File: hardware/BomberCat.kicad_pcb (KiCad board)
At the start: 2 copper layers, 0 parts

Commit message: add footprint memory and fix path footprints
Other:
- net class Default removed
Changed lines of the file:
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@@
-(kicad_pcb (version 20171130) (host pcbnew "(5.1.9-0-10_14)")
+(kicad_pcb (version 20211014) (generator pcbnew)
   (general
     (thickness 1.6)
-    (drawings 0)
-    (tracks 0)
-    (zones 0)
-    (modules 0)
-    (nets 1)
   )
-  (page A4)
+  (paper "A4")
   (layers
-    (0 Top signal)
-    (31 Bottom signal)
-    (32 B.Adhes user)
-    (33 F.Adhes user)
-    (34 B.Paste user)
-    (35 F.Paste user)
-    (36 B.SilkS user)
-    (37 F.SilkS user)
-    (38 B.Mask user)
-    (39 F.Mask user)
-    (40 Dwgs.User user)
-    (41 Cmts.User user)
-    (42 Eco1.User user)
-    (43 Eco2.User user)
-    (44 Edge.Cuts user)
-    (45 Margin user)
-    (46 B.CrtYd user)
-    (47 F.CrtYd user)
-    (48 B.Fab user)
-    (49 F.Fab user)
+    (0 "F.Cu" signal "Top")
+    (31 "B.Cu" signal "Bottom")
+    (32 "B.Adhes" user "B.Adhesive")
+    (33 "F.Adhes" user "F.Adhesive")
+    (34 "B.Paste" user)
+    (35 "F.Paste" user)
+    (36 "B.SilkS" user "B.Silkscreen")
+    (37 "F.SilkS" user "F.Silkscreen")
+    (38 "B.Mask" user)
+    (39 "F.Mask" user)
+    (40 "Dwgs.User" user "User.Drawings")
+    (41 "Cmts.User" user "User.Comments")
+    (42 "Eco1.User" user "User.Eco1")
+    (43 "Eco2.User" user "User.Eco2")
+    (44 "Edge.Cuts" user)
+    (45 "Margin" user "Margen")
+    (46 "B.CrtYd" user "B.Courtyard")
+    (47 "F.CrtYd" user "F.Courtyard")
+    (48 "B.Fab" user)
+    (49 "F.Fab" user)
   )
   (setup
-    (last_trace_width 0.2)
-    (user_trace_width 0.2)
-    (user_trace_width 0.25)
-    (user_trace_width 0.3)
-    (user_trace_width 0.4)
-    (user_trace_width 0.5)
-    (user_trace_width 0.6)
-    (user_trace_width 1)
-    (trace_clearance 0.2)
-    (zone_clearance 0.508)
-    (zone_45_only no)
-    (trace_min 0.1524)
-    (via_size 0.6)
-    (via_drill 0.3)
-    (via_min_size 0.6)
-    (via_min_drill 0.3)
-    (user_via 0.6 0.3)
-    (user_via 0.8 0.4)
-    (uvia_size 0.6)
-    (uvia_drill 0.3)
-    (uvias_allowed no)
-    (uvia_min_size 0.2)
-    (uvia_min_drill 0.1)
-    (edge_width 0.15)
-    (segment_width 0.2)
-    (pcb_text_width 0.3)
-    (pcb_text_size 1.5 1.5)
-    (mod_edge_width 0.15)
-    (mod_text_size 1 1)
-    (mod_text_width 0.15)
-    (pad_size 1.524 1.524)
-    (pad_drill 0.762)
     (pad_to_mask_clearance 0)
-    (aux_axis_origin 0 0)
-    (visible_elements 7FFFFFFF)
     (pcbplotparams
-      (layerselection 0x010fc_ffffffff)
+      (layerselection 0x00010fc_ffffffff)
+      (disableapertmacros false)
       (usegerberextensions false)
       (usegerberattributes false)
       (usegerberadvancedattributes false)
       (creategerberjobfile false)
+      (svguseinch false)
+      (svgprecision 6)
       (excludeedgelayer true)
-      (linewidth 0.100000)
       (plotframeref false)
       (viasonmask false)
@@
       (hpglpenspeed 20)
       (hpglpendiameter 15.000000)
+      (dxfpolygonmode true)
+      (dxfimperialunits true)
+      (dxfusepcbnewfont true)
       (psnegative false)
       (psa4output false)
@@
       (plotvalue true)
       (plotinvisibletext false)
-      (padsonsilk false)
+      (sketchpadsonfab false)
       (subtractmaskfromsilk false)
       (outputformat 1)
@@
       (drillshape 1)
       (scaleselection 1)
-      (outputdirectory ""))
+      (outputdirectory "")
+    )
   )
   (net 0 "")
-  (net_class Default "This is the default net class."
-    (clearance 0.2)
-    (trace_width 0.2)
-    (via_dia 0.6)
-    (via_drill 0.3)
-    (uvia_dia 0.6)
-    (uvia_drill 0.3)
-    (diff_pair_width 0.1524)
-    (diff_pair_gap 0.1524)
-  )
 )

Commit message: update component groups
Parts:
- added C1: 27pF, Capacitor_SMD:C_0603_1608Metric, F.Cu at (74.2, 79.9)
- added C10: 1uF, Capacitor_SMD:C_0603_1608Metric, F.Cu at (73.3, 97.8)
- added C11: 10uF, Capacitor_SMD:C_0603_1608Metric, F.Cu at (123.8, 31.2)
- added C12: 0.1uF, Capacitor_SMD:C_0603_1608Metric, F.Cu at (79.4, 97.7)
- added C13: 0.1uF, Capacitor_SMD:C_0603_1608Metric, F.Cu at (83.5, 97.8)
- added C14: 1uF, Capacitor_SMD:C_0603_1608Metric, F.Cu at (99.7, 83.8)
- added C15: 0.1uF, Capacitor_SMD:C_0603_1608Metric, F.Cu at (86.9, 97.8)
- added C16: 0.1uF, Capacitor_SMD:C_0603_1608Metric, F.Cu at (96.7, 83.9)
- added C17: 0.1uF, Capacitor_SMD:C_0603_1608Metric, F.Cu at (93.3, 98.1)
- added C18: 0.1uF, Capacitor_SMD:C_0603_1608Metric, F.Cu at (102.6, 84.0)
- added C19: 0.1uF, Capacitor_SMD:C_0603_1608Metric, F.Cu at (96.1, 98.2)
- added C2: 27pF, Capacitor_SMD:C_0603_1608Metric, F.Cu at (82.3, 79.8)
- added C20: 0.1uF, Capacitor_SMD:C_0603_1608Metric, F.Cu at (99.1, 98.2)
- added C21: 0.1uF, Capacitor_SMD:C_0603_1608Metric, F.Cu at (102.4, 98.2)
- added C22: 10uF, Capacitor_SMD:C_0603_1608Metric, F.Cu at (93.7, 31.5)
- added C23: 1nF/16V, Capacitor_SMD:C_0603_1608Metric, F.Cu at (186.8, 45.1)
- added C24: 1nF/16V, Capacitor_SMD:C_0603_1608Metric, F.Cu at (186.5, 53.9)
- added C25: 680pF, Capacitor_SMD:C_0603_1608Metric, F.Cu at (190.6, 45.8)
- added C26: 680pF, Capacitor_SMD:C_0603_1608Metric, F.Cu at (190.2, 53.2)
- added C27: 100pF/50V, Capacitor_SMD:C_0603_1608Metric, F.Cu at (191.3, 48.1)
- added C28: 100pF/50V, Capacitor_SMD:C_0603_1608Metric, F.Cu at (191.0, 50.9)
- added C29: 10uF, Capacitor_SMD:C_0603_1608Metric, F.Cu at (99.3, 31.5)
- added C3: 10pF, Capacitor_SMD:C_0603_1608Metric, F.Cu at (163.1, 59.6)
- added C30: 120pF, Capacitor_SMD:C_0603_1608Metric, F.Cu at (193.6, 47.3)
- added C31: 120pF, Capacitor_SMD:C_0603_1608Metric, F.Cu at (193.3, 51.7)
- added C32: 0.1uF, Capacitor_SMD:C_0603_1608Metric, F.Cu at (106.1, 98.0)
- added C33: 0.1uF, Capacitor_SMD:C_0603_1608Metric, F.Cu at (70.9, 61.6)
- added C34: 10uf, Capacitor_SMD:C_0603_1608Metric, F.Cu at (133.4, 48.1)
- added C4: 10pF, Capacitor_SMD:C_0603_1608Metric, F.Cu at (163.1, 55.5)
- added C5: 1uF, Capacitor_SMD:C_0603_1608Metric, F.Cu at (168.4, 49.3)
- added C6: 1uF, Capacitor_SMD:C_0603_1608Metric, F.Cu at (170.6, 67.5)
- added C7: 100nF, Capacitor_SMD:C_0603_1608Metric, F.Cu at (177.6, 55.8)
- added C8: 1uF, Capacitor_SMD:C_0603_1608Metric, F.Cu at (177.6, 57.3)
- added C9: 100nF, Capacitor_SMD:C_0603_1608Metric, F.Cu at (172.1, 67.5)
- added D1: LED, LED_SMD:LED_0805_2012Metric_Pad1.15x1.40mm_HandSolder, F.Cu at (126.9, 24.3)
- added D2: LED, LED_SMD:LED_0805_2012Metric_Pad1.15x1.40mm_HandSolder, F.Cu at (50.6, 100.9)
- added D3: LED, LED_SMD:LED_0805_2012Metric_Pad1.15x1.40mm_HandSolder, F.Cu at (90.3, 67.3)
- added D4: MBR120, Diode_SMD:D_SOD-123F, F.Cu at (90.7, 31.2)
- added F1: 0.5A, Fuse:Fuse_0603_1608Metric_Pad1.05x0.95mm_HandSolder, F.Cu at (81.6, 26.6)
- added H1: MountingHole, MountingHole:MountingHole_2.2mm_M2, F.Cu at (109.5, 122.4)
- added H2: MountingHole, MountingHole:MountingHole_2.2mm_M2, F.Cu at (115.0, 122.7)
- added H3: MountingHole, MountingHole:MountingHole_2.2mm_M2, F.Cu at (110.9, 130.6)
- added H4: MountingHole, MountingHole:MountingHole_2.2mm_M2, F.Cu at (124.1, 128.3)
- added J1: Battery, Connector_PinSocket_2.54mm:PinSocket_2x01_P2.54mm_Vertical_SMD, F.Cu at (118.2, 30.8)
- added J2: SWD, Connector:Tag-Connect_TC2030-IDC-NL_2x03_P1.27mm_Vertical, F.Cu at (73.1, 113.1)
- added J3: MAGSPOOF, Connector_PinHeader_2.54mm:PinHeader_1x02_P2.54mm_Vertical, F.Cu at (141.6, 43.6)
- added L1: 160nH, Inductor_SMD:L_0603_1608Metric_Pad1.05x0.95mm_HandSolder, F.Cu at (186.6, 48.1)
- added L2: 160nH, Inductor_SMD:L_0603_1608Metric_Pad1.05x0.95mm_HandSolder, F.Cu at (186.4, 50.9)
- added P1: USB_C_Plug_USB2.0, Connectors:C393939, F.Cu at (73.7, 30.2)
- added Q1: DMG3415U-7, Package_TO_SOT_SMD:SOT-23, F.Cu at (91.2, 28.1)
- added R1: 10K, Resistor_SMD:R_0603_1608Metric, F.Cu at (171.1, 63.6)
- added R10: 27, Resistor_SMD:R_0603_1608Metric, F.Cu at (79.3, 61.7)
- added R11: 1K, Resistor_SMD:R_0603_1608Metric, F.Cu at (125.2, 24.7)
- added R12: 1K, Resistor_SMD:R_0603_1608Metric, F.Cu at (50.6, 104.5)
- added R13: 1K, Resistor_SMD:R_0603_1608Metric, F.Cu at (94.0, 67.2)
- added R14: 100K, Resistor_SMD:R_0603_1608Metric, F.Cu at (91.4, 33.1)
- added R15: 2k2, Resistor_SMD:R_0603_1608Metric, F.Cu at (189.1, 47.3)
- added R16: 2k2, Resistor_SMD:R_0603_1608Metric, F.Cu at (188.8, 51.7)
- added R17: 10K, Resistor_SMD:R_0603_1608Metric, F.Cu at (40.9, 100.6)
- added R18: 3.24R, Resistor_SMD:R_0603_1608Metric, F.Cu at (197.8, 47.9)
- added R19: 3.24R, Resistor_SMD:R_0603_1608Metric, F.Cu at (198.3, 52.0)
- added R2: 10K, Resistor_SMD:R_0603_1608Metric, F.Cu at (172.6, 63.6)
- added R20: 10K, Resistor_SMD:R_0603_1608Metric, F.Cu at (69.4, 61.6)
- added R21: 100K, Resistor_SMD:R_0603_1608Metric, F.Cu at (167.2, 63.6)
- added R22: 100K, Resistor_SMD:R_0603_1608Metric, F.Cu at (168.6, 63.6)
- added R3: 1K, Resistor_SMD:R_0603_1608Metric, F.Cu at (82.2, 76.5)
- added R4: 5k1, Resistor_SMD:R_0603_1608Metric, F.Cu at (72.9, 24.2)
- added R5: 5k1, Resistor_SMD:R_0603_1608Metric, F.Cu at (73.4, 36.4)
- added R6: 100K, Resistor_SMD:R_0603_1608Metric, F.Cu at (118.6, 15.6)
- added R7: 100K, Resistor_SMD:R_0603_1608Metric, F.Cu at (118.6, 17.1)
- added R8: 1K, Resistor_SMD:R_0603_1608Metric, F.Cu at (127.1, 28.3)
- added R9: 27, Resistor_SMD:R_0603_1608Metric, F.Cu at (80.8, 61.7)
- added SW1: RESET, Button_Switch_SMD:SW_SPST_TL3342, F.Cu at (123.4, 87.0)
- added SW2: GPIO, Button_Switch_SMD:SW_SPST_TL3342, F.Cu at (123.4, 76.6)
- added U1: PN7150B0HN_C11002E-PN7150B0HN_C11002E, Package_DFN_QFN:QFN-40-1EP_6x6mm_P0.5mm_EP4.6x4.6mm, F.Cu at (170.3, 56.6)
- added U2: RP2040, BomberCat:RP2040-QFN-56, F.Cu at (78.8, 70.1)
- added U3: MCP73831-3-OT, Package_TO_SOT_SMD:SOT-23-5, F.Cu at (126.6, 30.8)
- added U4: AP2112K-3.3, Package_TO_SOT_SMD:SOT-23-5, F.Cu at (96.5, 31.7)
- added U5: ESP32-WROOM-32D, RF_Module:ESP32-WROOM-32, F.Cu at (47.6, 87.2)
- added U6: W25Q16JV, BomberCat:W25Q16JVUUIQ, F.Cu at (73.9, 62.0)
- added U7: TC4424, Package_SO:SOIC-8_3.9x4.9mm_P1.27mm, F.Cu at (135.6, 44.7)
- added Y1: 27.12Mhz, Crystal:Crystal_SMD_2016-4Pin_2.0x1.6mm, F.Cu at (163.2, 57.6)
- added Y2: 12Mhz, Crystal:Crystal_SMD_5032-2Pin_5.0x3.2mm, F.Cu at (78.3, 78.8)

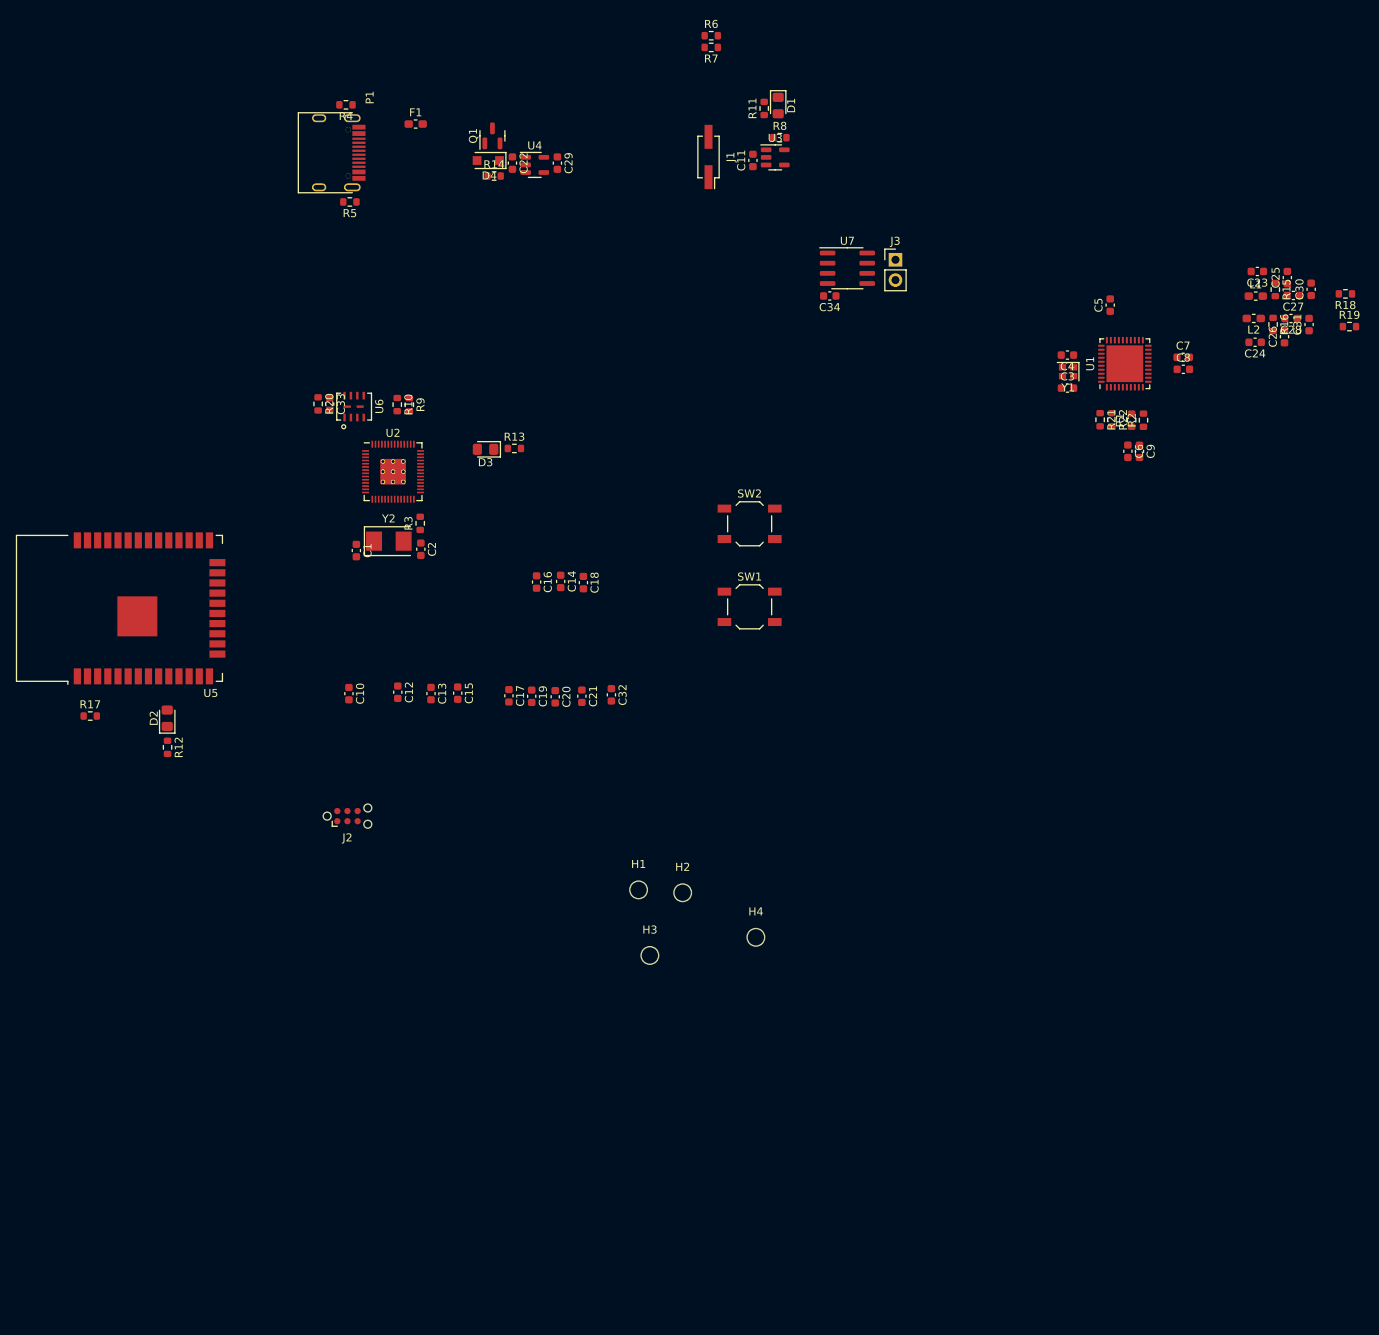
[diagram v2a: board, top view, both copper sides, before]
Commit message: Add grouped blocks for floorplan
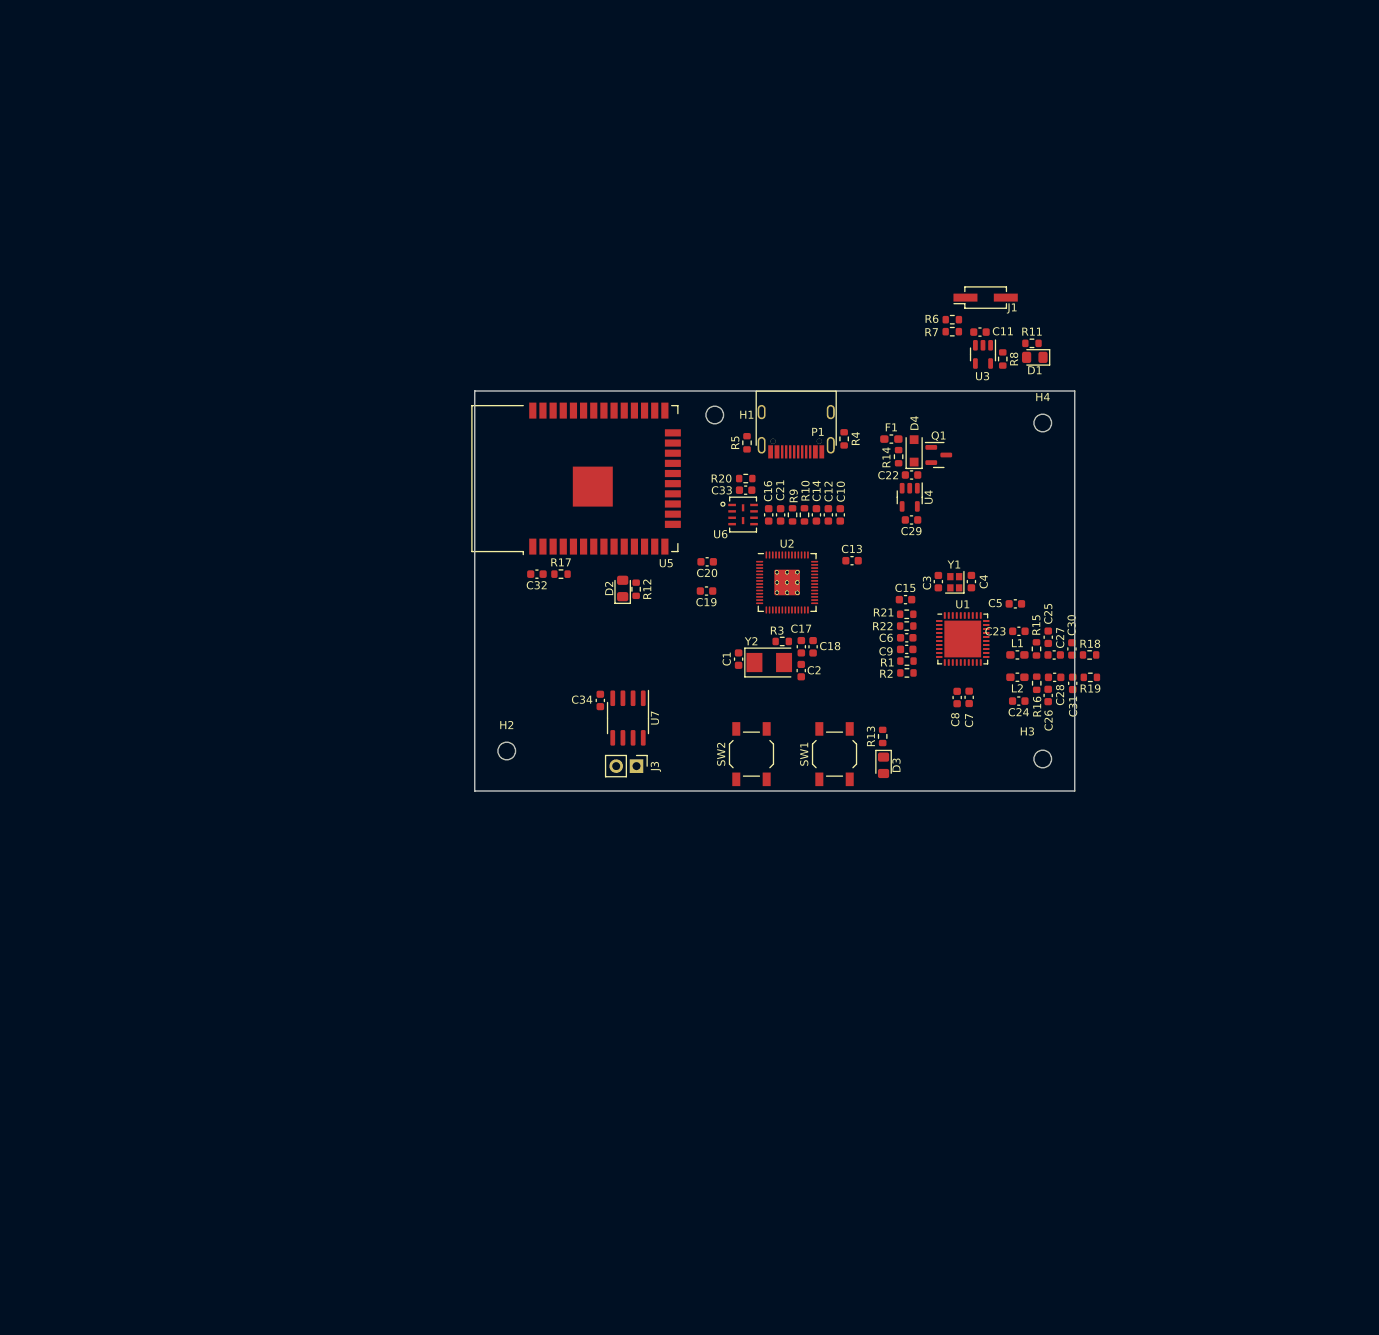
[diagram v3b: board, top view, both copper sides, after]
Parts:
- removed J2: SWD, Connector:Tag-Connect_TC2030-IDC-NL_2x03_P1.27mm_Vertical
- U1: value PN7150B0HN_C11002E-PN7150B0HN_C11002E -> PN7150B0HN_C11002E
- moved R4 75.0 mm to (135.2, 66.0), turned to 90 degrees
- moved H4 73.6 mm to (160.0, 64.0)
- moved F1 71.3 mm to (141.1, 66.0)
- moved J3 71.1 mm to (109.2, 106.9), turned to -90 degrees
- moved Q1 68.6 mm to (147.0, 68.0), turned to 0 degrees
- moved P1 66.4 mm to (129.2, 66.8), turned to 180 degrees
- moved C10 65.4 mm to (134.7, 75.5), turned to 90 degrees
- moved D4 64.4 mm to (143.9, 67.5), turned to 90 degrees
- moved D3 63.5 mm to (140.1, 106.8), turned to -90 degrees
- moved C22 63.3 mm to (143.6, 70.5), turned to 180 degrees
- moved C29 62.8 mm to (143.6, 76.1), turned to 180 degrees
- moved U4 62.6 mm to (143.4, 73.3), turned to -90 degrees
- moved U7 62.6 mm to (108.2, 100.9), turned to -90 degrees
- moved R12 61.8 mm to (109.2, 84.8)
- moved R14 61.5 mm to (142.0, 68.2), turned to -90 degrees
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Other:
- board outline added: 75 x 50 mm

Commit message: floorplan
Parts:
- U5: moved to B.Cu
- moved R6 119.3 mm to (137.3, 169.8), turned to -90 degrees
- moved J1 117.7 mm to (155.8, 166.0), turned to 90 degrees
- moved R7 117.6 mm to (138.8, 169.8), turned to 90 degrees
- moved C11 116.4 mm to (147.6, 169.0), turned to -90 degrees
- moved R8 115.0 mm to (141.3, 170.1), turned to 180 degrees
- moved U3 114.0 mm to (144.8, 169.2), turned to 180 degrees
- moved D1 110.3 mm to (151.6, 165.9)
- moved R11 110.3 mm to (151.2, 164.1)
- moved F1 100.0 mm to (147.6, 165.8), turned to -90 degrees
- moved D4 99.7 mm to (141.6, 167.2), turned to -90 degrees
- moved Q1 99.0 mm to (138.6, 166.6), turned to 180 degrees
- moved R14 97.8 mm to (143.6, 166.0), turned to 90 degrees
- moved R4 97.7 mm to (151.5, 162.3), turned to 0 degrees
- moved C22 92.5 mm to (143.6, 163.0), turned to -90 degrees
- moved P1 92.1 mm to (150.7, 156.3), turned to 90 degrees
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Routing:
- net +3V3: track 0.00 -> 36.7 mm, vias 0 -> 1
- net /SDA: track 0.00 -> 30.2 mm, vias 0 -> 2
- net /CS_RX: track 0.00 -> 29.8 mm
- net /SCL: track 0.00 -> 29.3 mm
- net +1V2: track 0.00 -> 26.7 mm
- net /COPI_RTS: track 0.00 -> 23.7 mm
- net /ESP_LED: track 0.00 -> 19.6 mm
- net /ACK_CTS: track 0.00 -> 18.4 mm
- net /CIPO_TX: track 0.00 -> 16.2 mm
- net GND: track 0.00 -> 15.5 mm, vias 0 -> 2
- net /QSPI_CS: track 0.00 -> 11.7 mm
- net /SCK: track 0.00 -> 9.52 mm, vias 0 -> 1
- net Net-(C1-Pad1): track 0.00 -> 9.52 mm
- net /QSPI_DATA1: track 0.00 -> 8.15 mm
- net /QSPI_DATA2: track 0.00 -> 7.15 mm
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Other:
- board size 75 x 50 mm -> 65 x 38 mm
